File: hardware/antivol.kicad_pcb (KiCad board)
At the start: 2 copper layers, 37.5 x 20.3 mm, 18 parts, among them J1 Conn_01x02, J2 Conn_01x06, J3 Conn_01x07, U1 ESP32-WROOM-32D, U2 MPU-6050, U3 SY8089AAAC(SOT23-5)

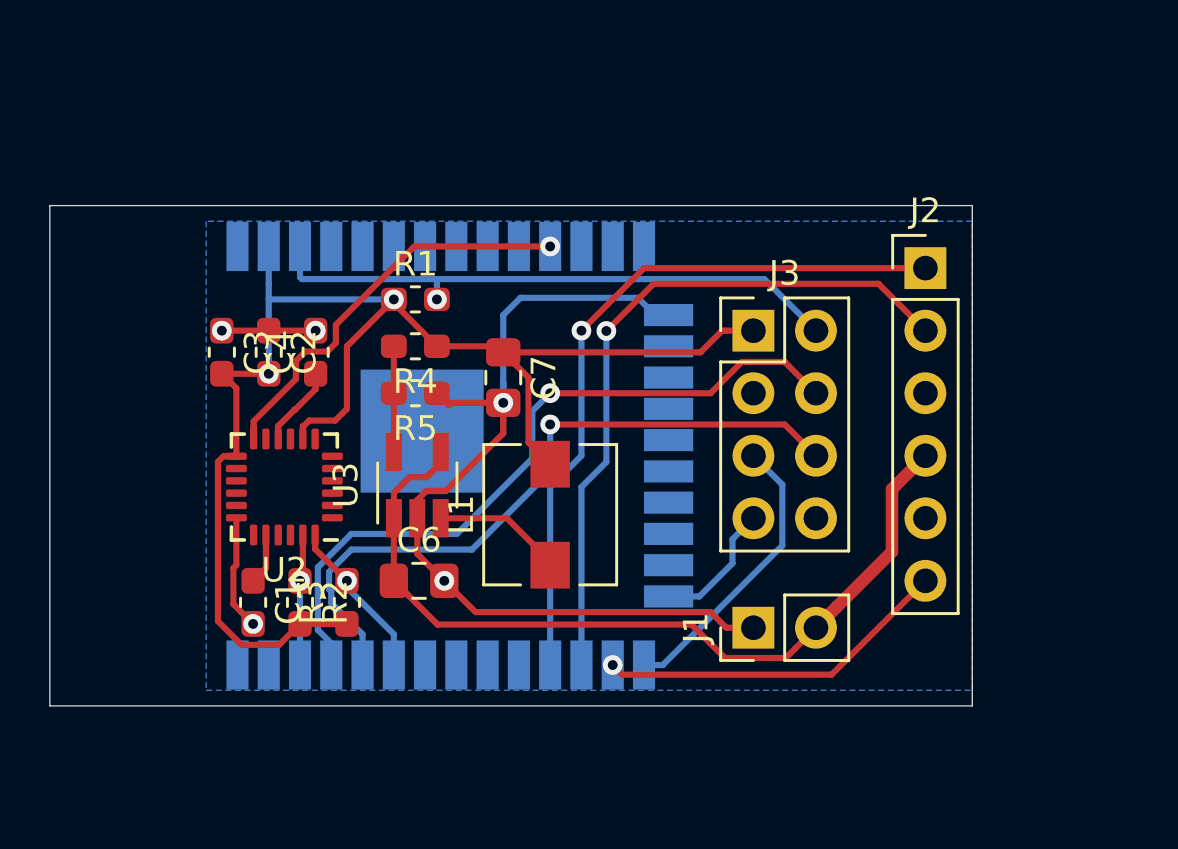
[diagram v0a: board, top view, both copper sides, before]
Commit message: Add charger
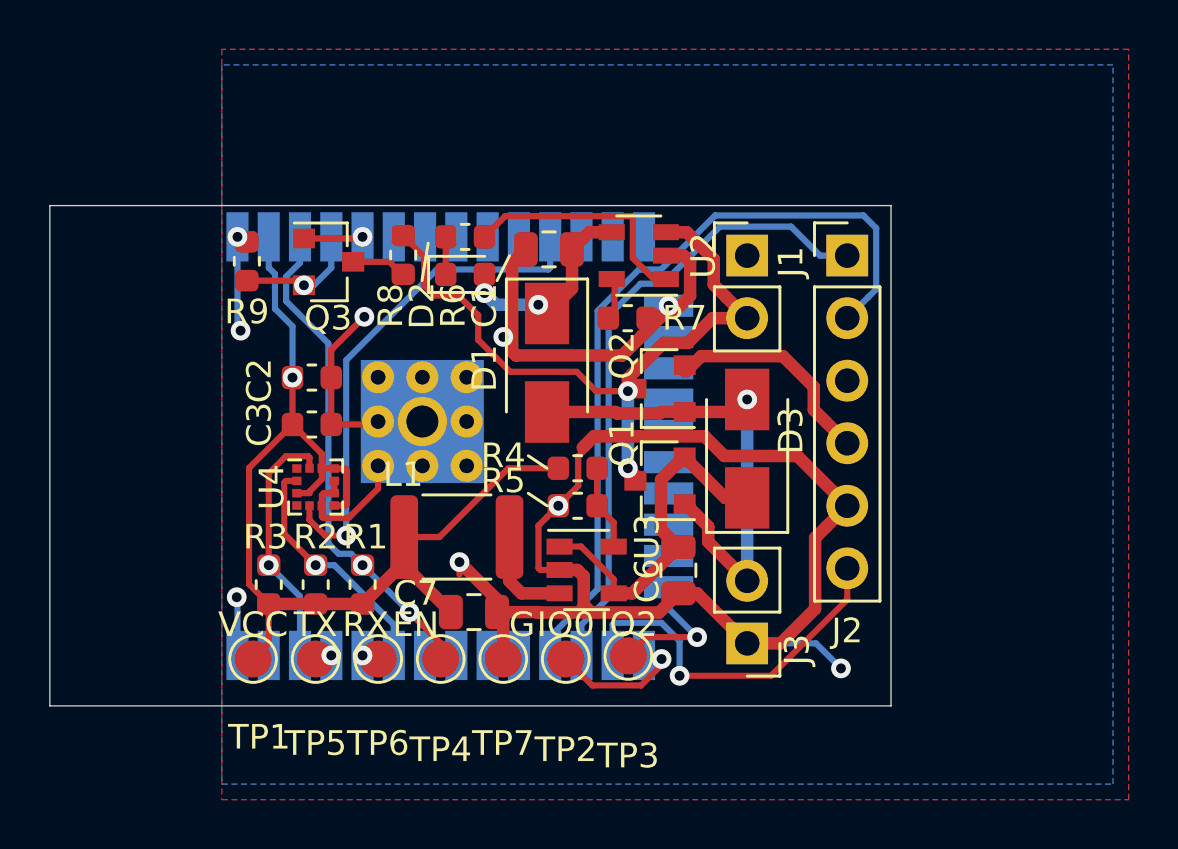
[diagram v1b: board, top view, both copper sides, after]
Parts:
- removed C4: 0.1µF, Capacitor_SMD:C_0603_1608Metric_Pad1.05x0.95mm_HandSolder
- added D1: SS14, Diode_SMD:D_SMA, F.Cu at (64.0, 104.2)
- added D2: LED, Diode_SMD:D_0603_1608Metric, F.Cu at (60.7, 100.6)
- added D3: SS14, Diode_SMD:D_SMA, F.Cu at (72.1, 107.7)
- added Q1: AO3401A, Package_TO_SOT_SMD:SOT-23, F.Cu at (68.6, 109.0)
- added Q2: AO3401A, Package_TO_SOT_SMD:SOT-23, F.Cu at (68.6, 105.2)
- added Q3: 2N7002, Package_TO_SOT_SMD:SOT-23, F.Cu at (55.1, 100.1)
- added R6: 2.2k, Resistor_SMD:R_0603_1608Metric, F.Cu at (60.7, 99.1)
- added R7: 2.2k, Resistor_SMD:R_0603_1608Metric, F.Cu at (67.3, 102.4)
- added R8: 10k, Resistor_SMD:R_0603_1608Metric, F.Cu at (58.2, 99.8)
- added R9: 10k, Resistor_SMD:R_0603_1608Metric, F.Cu at (51.8, 100.1)
- added TP1: TestPoint, TestPoint:TestPoint_Pad_D1.5mm, F.Cu at (52.1, 116.2)
- added TP2: TestPoint, TestPoint:TestPoint_Pad_D1.5mm, F.Cu at (64.8, 116.2)
- added TP3: TestPoint, TestPoint:TestPoint_Pad_D1.5mm, F.Cu at (67.3, 116.1)
- added TP4: TestPoint, TestPoint:TestPoint_Pad_D1.5mm, F.Cu at (59.7, 116.2)
- added TP5: TestPoint, TestPoint:TestPoint_Pad_D1.5mm, F.Cu at (54.6, 116.2)
- added TP6: TestPoint, TestPoint:TestPoint_Pad_D1.5mm, F.Cu at (57.1, 116.2)
- added TP7: TestPoint, TestPoint:TestPoint_Pad_D1.5mm, F.Cu at (62.2, 116.2)
- added U4: KXTJ3-1057, Package_LGA:LGA-12_2x2mm_P0.5mm, F.Cu at (54.6, 109.2)
- C1: value 2.2nF -> 47µF/6.3V; footprint Capacitor_SMD:C_0603_1608Metric_Pad1.05x0.95mm_HandSolder -> Capacitor_SMD:C_0805_2012Metric
- C2, C3: footprint Capacitor_SMD:C_0603_1608Metric_Pad1.05x0.95mm_HandSolder -> Capacitor_SMD:C_0603_1608Metric
- C6, C7: footprint Capacitor_SMD:C_0805_2012Metric_Pad1.15x1.40mm_HandSolder -> Capacitor_SMD:C_0805_2012Metric
- J3: value Conn_01x07 -> Conn_01x02; footprint Connector_PinHeader_2.54mm:PinHeader_2x04_P2.54mm_Vertical -> Connector_PinHeader_2.54mm:PinHeader_1x02_P2.54mm_Vertical
- L1: value 2.2µH/1.5A -> 15µH/450mA - NLC453232T-150K-PF; footprint Inductor_SMD:L_Wuerth_HCI-5040 -> Inductor_SMD:L_1812_4532Metric
- R1, R2, R3, R4, R5: footprint Resistor_SMD:R_0603_1608Metric_Pad1.05x0.95mm_HandSolder -> Resistor_SMD:R_0603_1608Metric
- U1: value ESP32-WROOM-32D -> ESP-WROOM-32; footprint RF_Module:ESP32-WROOM-32 -> OLIMEX_Cases-FP:ESP-WROOM-32_MODULE
- U2: value MPU-6050 -> TP4054 (SOT23-5); footprint Sensor_Motion:InvenSense_QFN-24_4x4mm_P0.5mm -> Package_TO_SOT_SMD:SOT-23-5
- U3: footprint Package_TO_SOT_SMD:SOT-23-5_HandSoldering -> Package_TO_SOT_SMD:SOT-23-5
- moved C1 18.7 mm to (64.1, 99.6), turned to 180 degrees
- moved U2 17.2 mm to (67.7, 99.8)
- moved J1 15.1 mm to (72.1, 99.8), turned to 0 degrees
- moved J3 12.7 mm to (72.1, 115.6), turned to 180 degrees
- moved R1 11.8 mm to (56.5, 113.2), turned to 90 degrees
- moved C6 10.5 mm to (69.3, 112.6), turned to 270 degrees
- moved C7 9.60 mm to (61.0, 114.3), turned to 0 degrees
- moved R4 8.25 mm to (65.3, 108.5), turned to 0 degrees
- moved R5 8.02 mm to (65.3, 110.0), turned to 0 degrees
- moved U3 7.69 mm to (65.6, 112.6), turned to 0 degrees
- moved C3 4.69 mm to (54.5, 106.7), turned to 180 degrees
- moved L1 3.90 mm to (60.3, 111.3), turned to 180 degrees
- moved J2 3.22 mm to (76.2, 99.8)
- moved U1 2.97 mm to (56.7, 107.6)
- moved C2 2.03 mm to (54.5, 104.8), turned to 180 degrees
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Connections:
- C6 pad 1: +BATT -> Net-(C6-Pad1)
- J2 pad 3: Net-(J2-Pad3) -> (no net)
- J2 pad 4: +BATT -> /GSM_VBAT
- J3 pad 1: +3V3 -> GND
- J3 pad 2: /ESP_EN -> +5V_USB
- U1 pad 10: Net-(U1-Pad10) -> (no net)
- U1 pad 12: Net-(U1-Pad12) -> (no net)
- U1 pad 13: Net-(U1-Pad13) -> (no net)
- U1 pad 14: Net-(U1-Pad14) -> (no net)
- U1 pad 16: Net-(U1-Pad16) -> (no net)
- U1 pad 17: Net-(U1-Pad17) -> (no net)
- U1 pad 18: Net-(U1-Pad18) -> (no net)
- U1 pad 19: Net-(U1-Pad19) -> (no net)
- U1 pad 20: Net-(U1-Pad20) -> (no net)
- U1 pad 21: Net-(U1-Pad21) -> (no net)
- U1 pad 22: Net-(U1-Pad22) -> (no net)
- U1 pad 23: Net-(U1-Pad23) -> (no net)
- U1 pad 27: /GSM_RX -> /GSM_TX
- U1 pad 28: /GSM_TX -> /GSM_RX
- U1 pad 29: Net-(U1-Pad29) -> (no net)
- U1 pad 30: Net-(U1-Pad30) -> (no net)
- U1 pad 31: Net-(U1-Pad31) -> (no net)
- U1 pad 32: Net-(U1-Pad32) -> (no net)
- U1 pad 37: Net-(U1-Pad37) -> (no net)
- U1 pad 39: (no net) -> GND
- U1 pad 4: Net-(U1-Pad4) -> /ADC
- U1 pad 5: Net-(U1-Pad5) -> /ADC_EN
- U1 pad 6: Net-(U1-Pad6) -> (no net)
- U1 pad 7: Net-(U1-Pad7) -> (no net)
- U1 pad 8: Net-(U1-Pad8) -> (no net)
- U1 pad 9: Net-(U1-Pad9) -> (no net)
- U2 pad 2: (no net) -> GND
- U2 pad 3: (no net) -> +BATT
- U2 pad 4: (no net) -> Net-(C1-Pad1)
- U2 pad 5: (no net) -> Net-(R7-Pad2)
- U3 pad 1: +BATT -> Net-(C6-Pad1)
- U3 pad 4: +BATT -> Net-(C6-Pad1)
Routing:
- net GND: track 47.4 -> 85.8 mm, vias 5 -> 9
- net /ESP_TX: track 29.5 -> 0.70 mm
- net /ESP_RX: track 28.2 -> 0.70 mm
- net +5V_USB: track 0.00 -> 20.3 mm, vias 0 -> 1
- net Net-(C6-Pad1): track 0.00 -> 14.3 mm
- net +3V3: track 58.2 -> 44.5 mm, vias 2 -> 1
- net Net-(R6-Pad1): track 0.00 -> 9.73 mm
- net /GSM_VBAT: track 0.00 -> 8.87 mm
- net +BATT: track 35.1 -> 28.6 mm, vias 0 -> 2
- net Net-(C1-Pad1): track 2.08 -> 8.14 mm, vias 0 -> 2
- net /ESP_IO0: track 11.8 -> 5.70 mm, vias 0 -> 1
- net /ADC: track 0.00 -> 5.06 mm, vias 0 -> 1
- net /SCL: track 5.33 -> 10.3 mm
- net /GSM_RX: track 28.5 -> 32.1 mm
- net Net-(C4-Pad1): track 3.29 -> 0.00 mm
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- added copper zone on F.Cu, net GND
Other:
- board size 37.5 x 20.3 mm -> 34.2 x 20.3 mm
- net class Default: clearance 0.2 -> 0.1
- rule trace_clearance: 0.2 -> 0.1
- board text added: "EN"
- board text added: "G"
- board text added: "IO0"
- board text added: "IO2"
- board text added: "RX"
- board text added: "TX"
- board text added: "VCC"

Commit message: final without usb
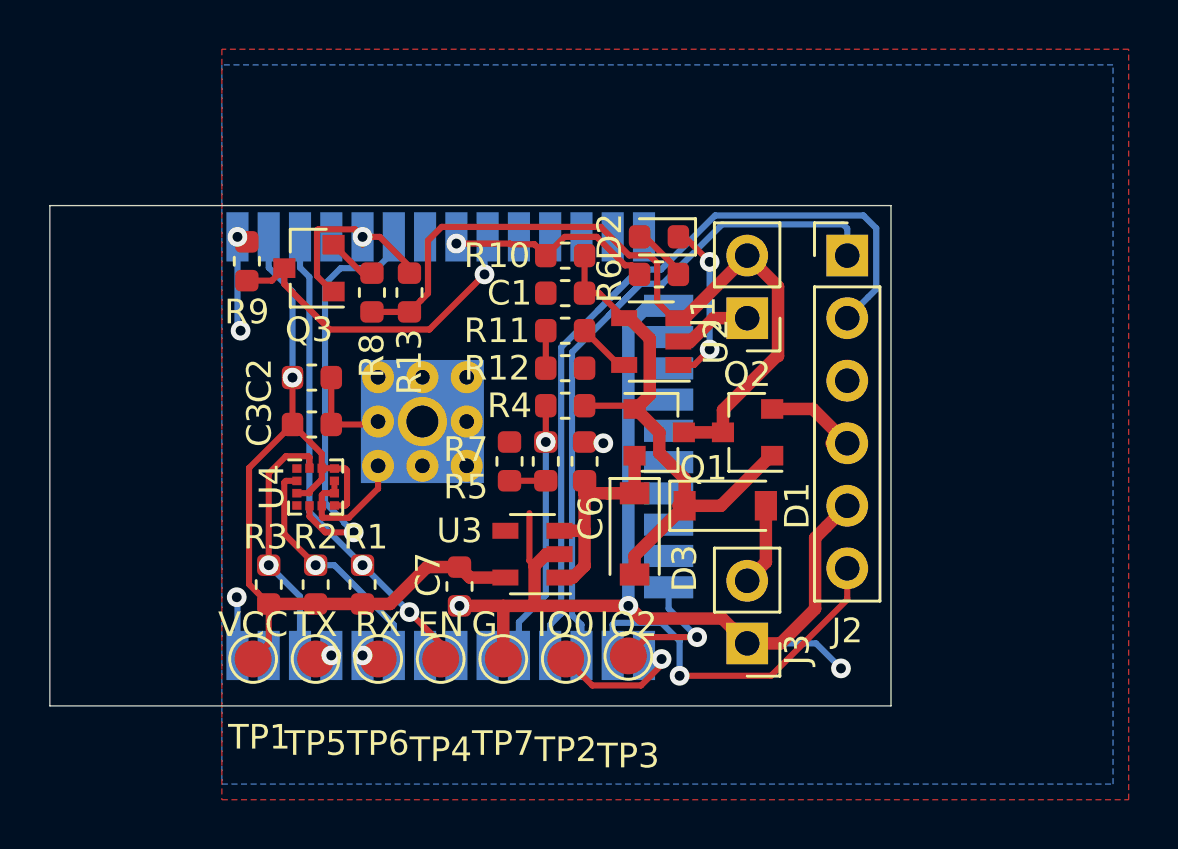
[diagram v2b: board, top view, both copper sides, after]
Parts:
- removed L1: 15µH/450mA - NLC453232T-150K-PF, Inductor_SMD:L_1812_4532Metric
- added R10: 1k, Resistor_SMD:R_0603_1608Metric, F.Cu at (64.7, 99.8)
- added R11: 1k, Resistor_SMD:R_0603_1608Metric, F.Cu at (64.7, 102.9)
- added R12: 1k, Resistor_SMD:R_0603_1608Metric, F.Cu at (64.7, 104.4)
- added R13: 10k, Resistor_SMD:R_0603_1608Metric, F.Cu at (58.4, 101.3)
- C1, C6, C7: value 47µF/6.3V -> 1µF/6.3V; footprint Capacitor_SMD:C_0805_2012Metric -> Capacitor_SMD:C_0603_1608Metric
- D1, D3: value SS14 -> B5819W; footprint Diode_SMD:D_SMA -> Diode_SMD:D_SOD-123
- Q3: value 2N7002 -> AO3401A
- R1: value 1K R0603 -> 1k
- R4: value 100k -> 10k
- R5: value 22k -> 10k
- R6: value 2.2k -> 1k
- R7: value 2.2k -> 10k
- U2: value TP4054 (SOT23-5) -> TP4054
- U3: value SY8089AAAC(SOT23-5) -> ME6211C33
- moved D1 9.28 mm to (71.2, 110.0), turned to 0 degrees
- moved D2 8.02 mm to (68.6, 99.1), turned to 180 degrees
- moved R6 8.02 mm to (68.6, 100.6)
- moved R7 7.54 mm to (62.5, 108.2), turned to 270 degrees
- moved C6 5.84 mm to (65.5, 108.2), turned to 90 degrees
- moved D3 5.73 mm to (67.6, 111.1), turned to 270 degrees
- moved Q2 3.98 mm to (72.2, 107.0)
- moved U2 3.53 mm to (68.2, 103.3)
- moved R4 2.59 mm to (64.7, 105.9), turned to 180 degrees
- moved J1 2.54 mm to (72.1, 102.4), turned to 180 degrees
- moved U3 2.29 mm to (63.4, 111.9), turned to 180 degrees
- moved R5 2.22 mm to (64.0, 108.2), turned to 90 degrees
- moved R8 1.98 mm to (56.9, 101.3), turned to 90 degrees
- moved Q1 1.97 mm to (68.6, 107.0), turned to 0 degrees
- moved C1 1.90 mm to (64.7, 101.3)
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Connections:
- C1 pad 1: Net-(C1-Pad1) -> +5V_USB
- D1 pad 1: Net-(C1-Pad1) -> +5V_USB
- D1 pad 2: +5V_USB -> Net-(D1-Pad2)
- D2 pad 2: Net-(C1-Pad1) -> Net-(D2-Pad2)
- J3 pad 2: +5V_USB -> Net-(D1-Pad2)
- Q3 pad 2: /ADC -> Net-(Q3-Pad2)
- Q3 pad 3: Net-(Q3-Pad3) -> /ADC
- R4 pad 1: +3V3 -> +5V_USB
- R4 pad 2: Net-(R4-Pad2) -> /USB_PWR
- R5 pad 1: GND -> Net-(R5-Pad1)
- R5 pad 2: Net-(R4-Pad2) -> /USB_PWR
- R6 pad 1: Net-(R6-Pad1) -> Net-(D2-Pad2)
- R6 pad 2: Net-(D2-Pad1) -> /CHARG
- R7 pad 2: Net-(R7-Pad2) -> Net-(R5-Pad1)
- R8 pad 2: Net-(Q3-Pad3) -> Net-(Q3-Pad2)
- U1 pad 11: /ACCEL_INT -> (no net)
- U1 pad 29: (no net) -> /USB_PWR
- U1 pad 4: /ADC -> (no net)
- U1 pad 6: (no net) -> /ACCEL_INT
- U1 pad 8: (no net) -> /CHARG
- U1 pad 9: (no net) -> /ADC
- U2 pad 1: Net-(R6-Pad1) -> Net-(D2-Pad1)
- U2 pad 4: Net-(C1-Pad1) -> +5V_USB
- U2 pad 5: Net-(R7-Pad2) -> Net-(R11-Pad2)
- U3 pad 3: Net-(L1-Pad1) -> Net-(C6-Pad1)
- U3 pad 4: Net-(C6-Pad1) -> (no net)
- U3 pad 5: Net-(R4-Pad2) -> +3V3
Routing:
- net GND: track 85.8 -> 65.1 mm, vias 9 -> 7
- net /USB_PWR: track 0.00 -> 11.1 mm, vias 0 -> 1
- net Net-(R6-Pad1): track 9.73 -> 0.00 mm
- net /ADC: track 5.06 -> 13.8 mm
- net /CHARG: track 0.00 -> 8.62 mm, vias 0 -> 1
- net Net-(C1-Pad1): track 8.14 -> 0.00 mm, vias 2 -> 0
- net +3V3: track 44.5 -> 36.7 mm
- net /ADC_EN: track 2.41 -> 7.77 mm
- net Net-(D2-Pad1): track 1.52 -> 6.88 mm, vias 0 -> 2
- net Net-(C6-Pad1): track 14.3 -> 9.24 mm
- net /GSM_VBAT: track 8.87 -> 4.26 mm
- net Net-(L1-Pad1): track 4.03 -> 0.00 mm
- net Net-(R4-Pad2): track 3.46 -> 0.00 mm
- net Net-(D1-Pad2): track 0.00 -> 3.36 mm
- net +BATT: track 28.6 -> 31.7 mm, vias 2 -> 0
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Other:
- net class POWER: clearance 0.254 -> 0.15

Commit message: v1
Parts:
- removed J3: Conn_01x02, Connector_PinHeader_2.54mm:PinHeader_1x02_P2.54mm_Vertical
- removed TP1, TP2, TP3, TP4, TP5, TP6, TP7: TestPoint, TestPoint:TestPoint_Pad_D1.5mm
- added C10: 0.1µF, Capacitor_SMD:C_0603_1608Metric, F.Cu at (66.6, 109.0)
- added C4: 1nF, Capacitor_SMD:C_0603_1608Metric, F.Cu at (53.6, 104.6)
- added C5: 12pF, Capacitor_SMD:C_0603_1608Metric, F.Cu at (65.9, 106.7)
- added C8: 12pF, Capacitor_SMD:C_0603_1608Metric, F.Cu at (63.3, 104.5)
- added C9: 10µF/25V, Capacitor_SMD:C_0805_2012Metric, F.Cu at (72.6, 115.7)
- added J4: USB_B_Micro, Connector_USB:USB_Micro-B_Molex-105017-0001, F.Cu at (79.0, 113.6)
- added Q4: S8050, Package_TO_SOT_SMD:SOT-23, F.Cu at (53.0, 107.2)
- added Q5: S8050, Package_TO_SOT_SMD:SOT-23, F.Cu at (57.7, 110.6)
- added R14: 470, Resistor_SMD:R_0603_1608Metric, F.Cu at (58.9, 115.3)
- added R15: 10k, Resistor_SMD:R_0603_1608Metric, F.Cu at (55.6, 107.2)
- added R16: 22k, Resistor_SMD:R_0603_1608Metric, F.Cu at (53.5, 99.3)
- added U5: CH340G, Package_SO:SOIC-16_3.9x9.9mm_P1.27mm, F.Cu at (65.5, 113.5)
- added Y1: 12MHz, Crystal:Crystal_SMD_3225-4Pin_3.2x2.5mm, F.Cu at (63.2, 107.4)
- C2: value 10nF -> 0.1µF
- R1, R11: value 1k -> 2.2k
- R12: value 1k -> 10k
- R13, R5: value 10k -> 22k
- R7: value 10k -> 470
- U3: value ME6211C33 -> XC6206P332; footprint Package_TO_SOT_SMD:SOT-23-5 -> Package_TO_SOT_SMD:SOT-23
- moved R13 17.2 mm to (75.5, 99.8)
- moved C1 14.2 mm to (78.7, 103.9), turned to 270 degrees
- moved U2 13.4 mm to (81.6, 103.5), turned to 270 degrees
- moved R12 13.0 mm to (52.9, 109.7)
- moved D3 12.8 mm to (79.9, 107.8), turned to 90 degrees
- moved R11 11.6 mm to (76.3, 102.2)
- moved D1 11.3 mm to (82.3, 107.8), turned to 270 degrees
- moved R1 10.5 mm to (53.6, 103.1), turned to 0 degrees
- moved U3 10.1 mm to (68.7, 103.4), turned to 0 degrees
- moved J1 9.80 mm to (81.5, 99.6), turned to 270 degrees
- moved C7 9.58 mm to (67.4, 106.7)
- moved C3 8.92 mm to (52.1, 115.3), turned to 90 degrees
- moved R7 8.70 mm to (57.4, 115.3)
- moved R5 8.28 mm to (62.4, 100.1)
- moved Q1 7.76 mm to (76.2, 108.3)
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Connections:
- Q2 pad 1: +5V_USB -> /GSM_PWR
- Q2 pad 2: /GSM_VBAT -> +BATT
- Q2 pad 3: +BATT -> /GSM_VBAT
- R1 pad 1: +3V3 -> /ESP_EN
- R1 pad 2: /ESP_EN -> +3V3
- R11 pad 1: Net-(R11-Pad1) -> GND
- R12 pad 1: GND -> Net-(Q5-Pad2)
- R12 pad 2: Net-(R11-Pad1) -> Net-(Q4-Pad1)
- R13 pad 1: +BATT -> /GSM_PWR
- R13 pad 2: /ADC_EN -> +BATT
- R5 pad 1: Net-(R5-Pad1) -> GND
- R7 pad 1: GND -> /ESP_RX
- R7 pad 2: Net-(R5-Pad1) -> Net-(R7-Pad2)
- U1 pad 10: (no net) -> /USB_PWR
- U1 pad 13: (no net) -> /CHARG
- U1 pad 14: (no net) -> /GSM_PWR
- U1 pad 24: /ESP_IO2 -> /GSM_KEY
- U1 pad 26: /GSM_KEY -> (no net)
- U1 pad 29: /USB_PWR -> (no net)
- U1 pad 4: (no net) -> /ACCEL_INT
- U1 pad 5: /ADC_EN -> (no net)
- U1 pad 6: /ACCEL_INT -> (no net)
- U1 pad 8: /CHARG -> /ADC_EN
- U3 pad 1: Net-(C6-Pad1) -> GND
- U3 pad 2: GND -> +3V3
- U4 pad 1: (no net) -> GND
- U4 pad 4: (no net) -> GND
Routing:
- net GND: track 65.1 -> 127.7 mm, vias 7 -> 8
- net +3V3: track 36.7 -> 60.9 mm, vias 1 -> 3
- net Net-(R7-Pad2): track 0.00 -> 24.1 mm
- net Net-(Q4-Pad2): track 0.00 -> 20.6 mm, vias 0 -> 2
- net /USB_D+: track 0.00 -> 19.2 mm, vias 0 -> 2
- net /USB_D-: track 0.00 -> 18.8 mm, vias 0 -> 2
- net Net-(Q5-Pad2): track 0.00 -> 16.6 mm, vias 0 -> 3
- net Net-(D2-Pad1): track 6.88 -> 22.0 mm, vias 2 -> 0
- net /GSM_PWR: track 0.00 -> 13.0 mm, vias 0 -> 1
- net +BATT: track 31.7 -> 43.9 mm, vias 0 -> 2
- net Net-(R14-Pad2): track 0.00 -> 11.7 mm
- net /GSM_KEY: track 15.2 -> 4.17 mm, vias 1 -> 0
- net /GSM_RX: track 34.4 -> 23.8 mm
- net /ESP_EN: track 21.3 -> 11.4 mm, vias 2 -> 1
- net +5V_USB: track 22.9 -> 31.7 mm, vias 0 -> 2
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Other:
- board size 34.2 x 20.3 mm -> 39.8 x 20.3 mm
- board text added: "ANTIVOL 1.0 puyb.net"
- board text removed: "EN"
- board text removed: "G"
- board text removed: "IO0"
- board text removed: "IO2"
- board text removed: "RX"
- board text removed: "TX"
- board text removed: "VCC"
